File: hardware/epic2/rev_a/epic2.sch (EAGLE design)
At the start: 35 parts, among them J1 EPIC2-HEADER2, U2 FM25LBTDFN-8, U3 CC2538, U5 RV-3049-C3, X1 EPSON-FA-128, X3 ABS05-32.768KHZ-T

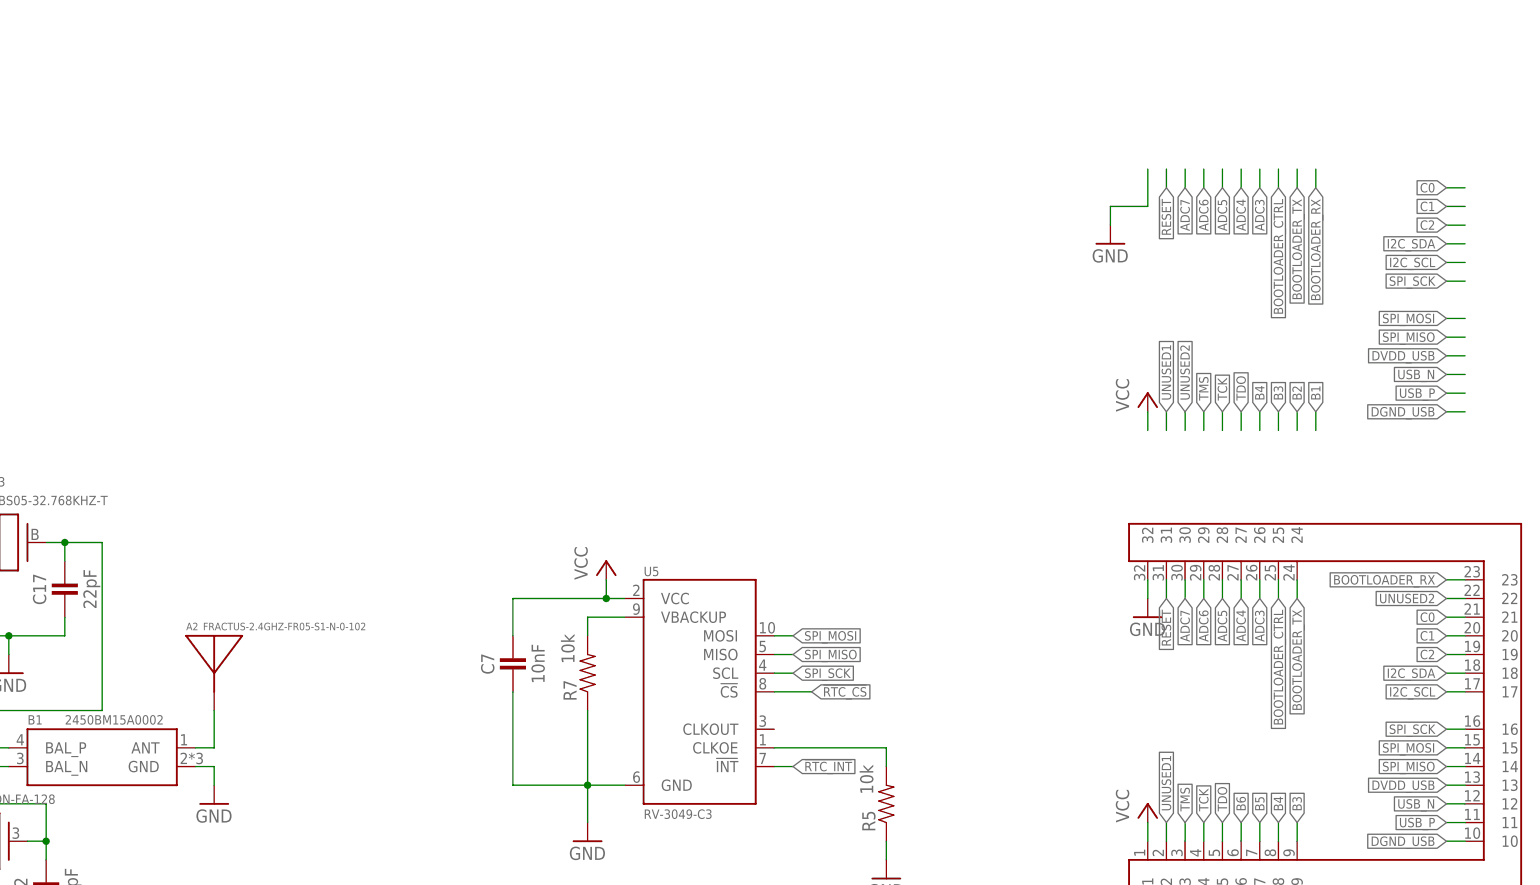
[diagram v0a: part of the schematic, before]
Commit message: epic2/myth routed
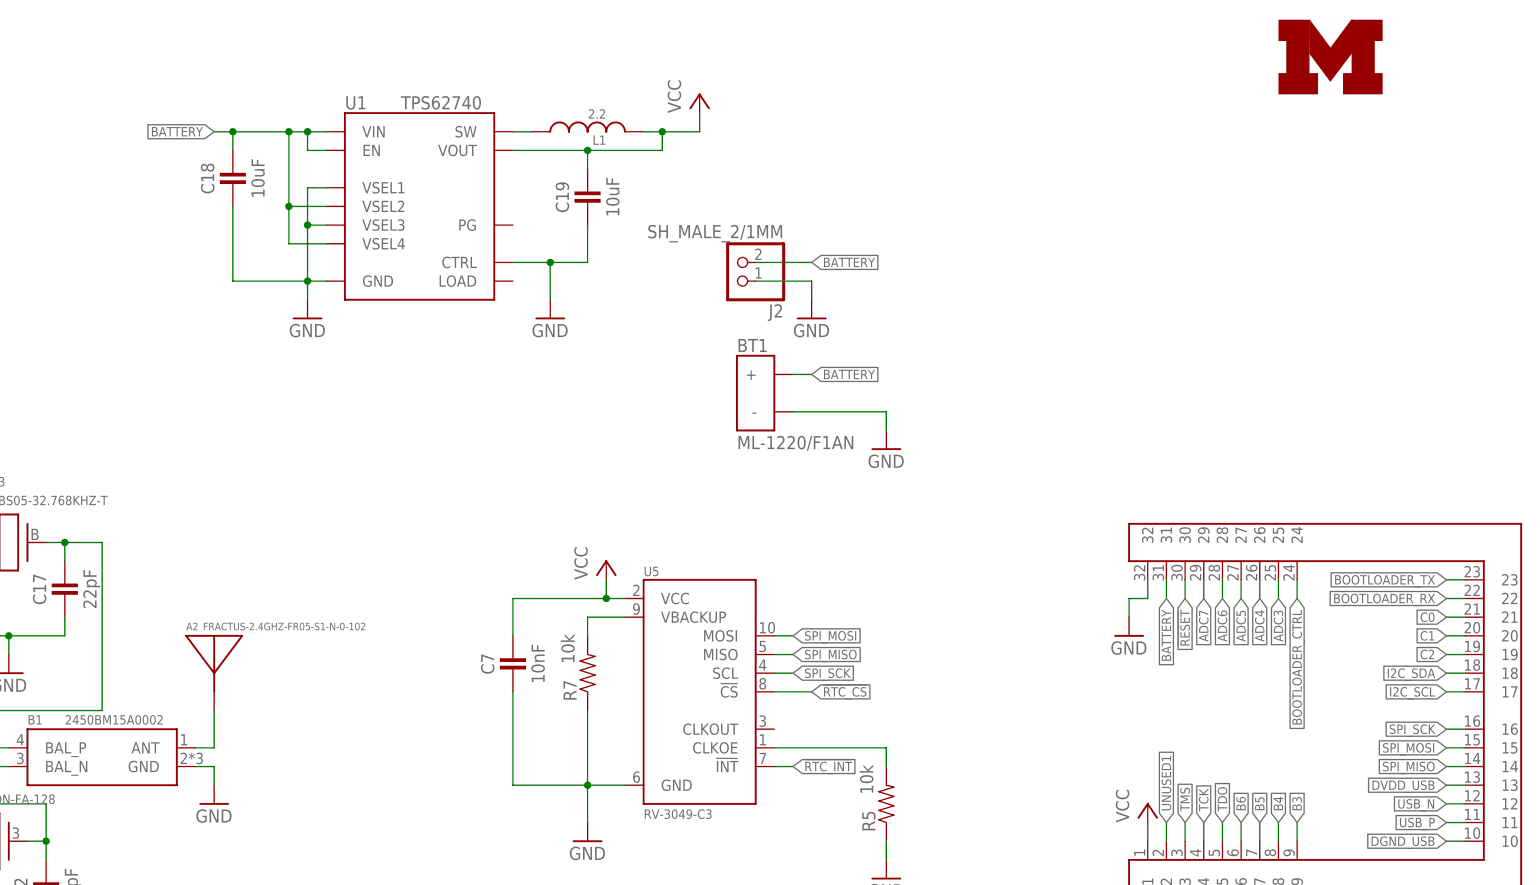
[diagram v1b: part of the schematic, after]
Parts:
- added BT1: ML-1220/F1AN, batteries:ML-1220/F1AN
- added C18, C19: 10uF, passives:CAPACITOR0603_CAP
- added J2: SH_MALE_2/1MM, headers:SH_MALE_2/1MM
- added L1: 2.2, passives:MIPSZ2012D
- added LOGO1: UMICH_SOLID_TINY, logos:UMICH_SOLID_TINY
- added U1: TPS62740, chips:TPS62740
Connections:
- removed net UNUSED2: J1.22
- new net BATTERY: BT1.+, C18.1, J1.31, J2.2, U1.EN, U1.VIN, U1.VSEL2, U1.VSEL4
- new net N$5: L1.1, U1.SW
- net !RESET: now also J1.30; no longer J1.31
- net ADC3: now also J1.25; no longer J1.26
- net ADC4: now also J1.26; no longer J1.27
- net ADC5: now also J1.27; no longer J1.28
- net ADC6: now also J1.28; no longer J1.29
- net ADC7: now also J1.29; no longer J1.30
- net BOOTLOADER_CTRL: now also J1.24; no longer J1.25
- net BOOTLOADER_RX: now also J1.22; no longer J1.23
- net BOOTLOADER_TX: now also J1.23; no longer J1.24
- net GND: now also BT1.-, C18.2, C19.2, J2.1, U1.CTRL, U1.GND, U1.VSEL1, U1.VSEL3
- net VCC: now also C19.1, L1.2, U1.VOUT
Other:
- note added: "2.8V Output"

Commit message: updated epic2 brd
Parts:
- removed U$1: UMICH_SOLID_SMALL, logos:UMICH_SOLID_SMALL
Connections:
- removed net !RTC_CS: U3.PB1, U5.!CS
- new net RTC_CE: U3.PB1, U5.CE
